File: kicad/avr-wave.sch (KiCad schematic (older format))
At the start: 57 parts, among them J1 MIDI_IN, J2 AVR-ISP-6, J3 MAIN_CONN, J4 ADC_CONN, J5 LINE_OUT, U1 L78L05_SO8, U2 6N137, U3 ATmega328-AU, U4 MCP4921, U5 MCP6001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

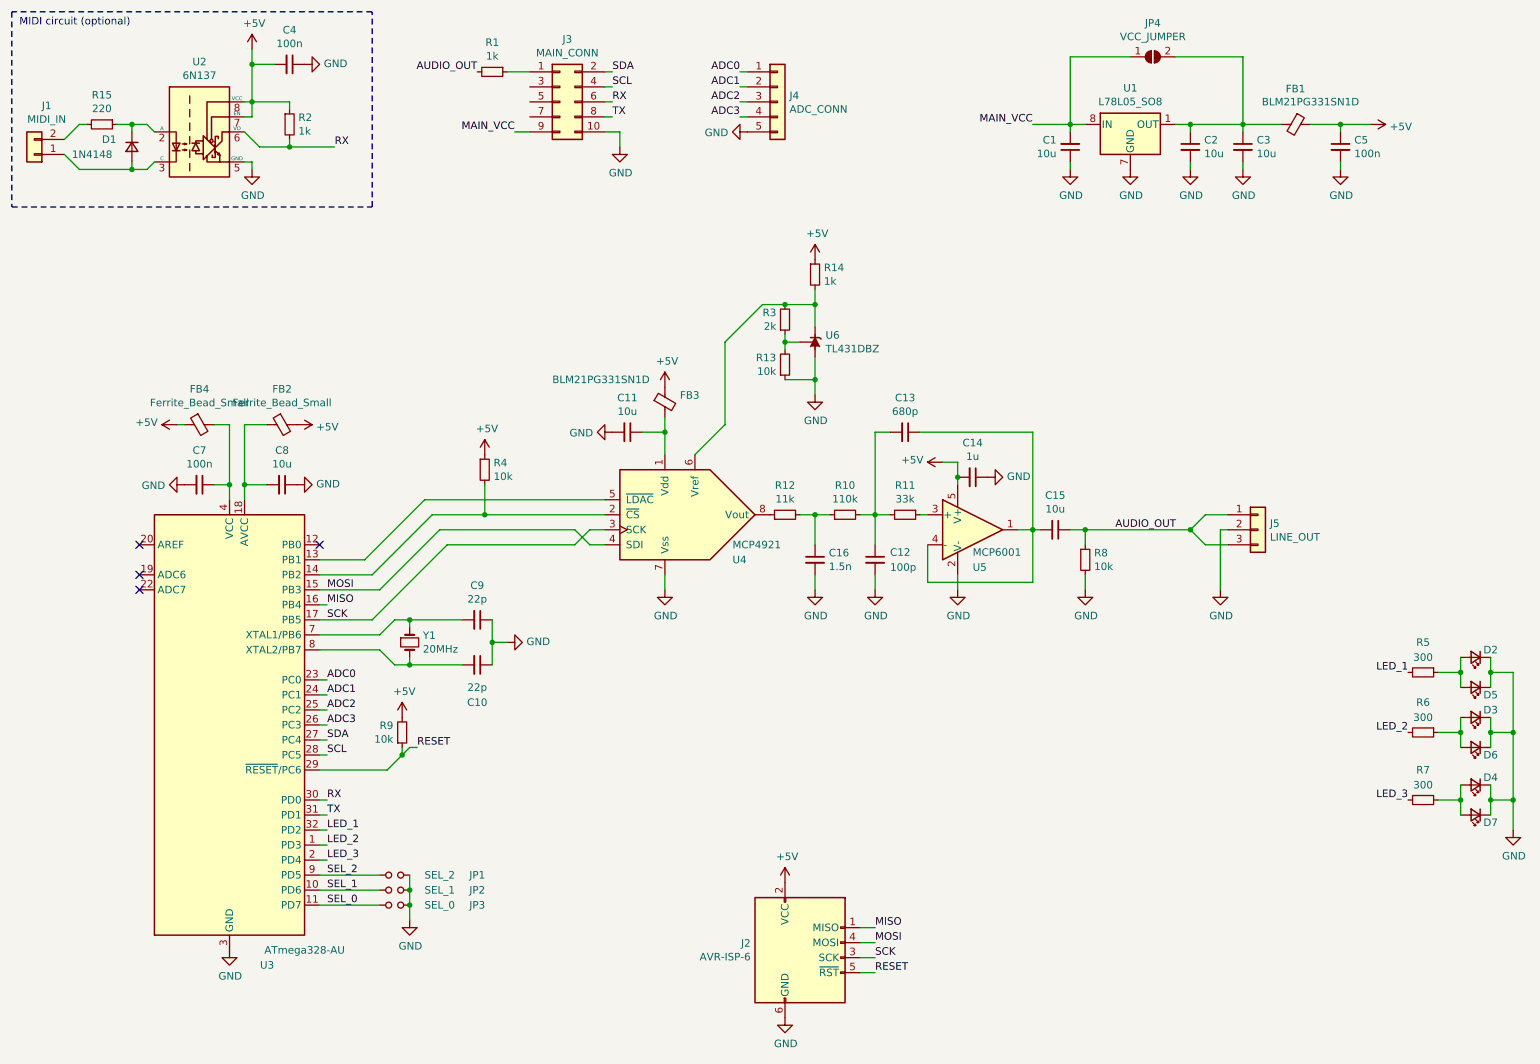
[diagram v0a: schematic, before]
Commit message: Improve power supply filtering
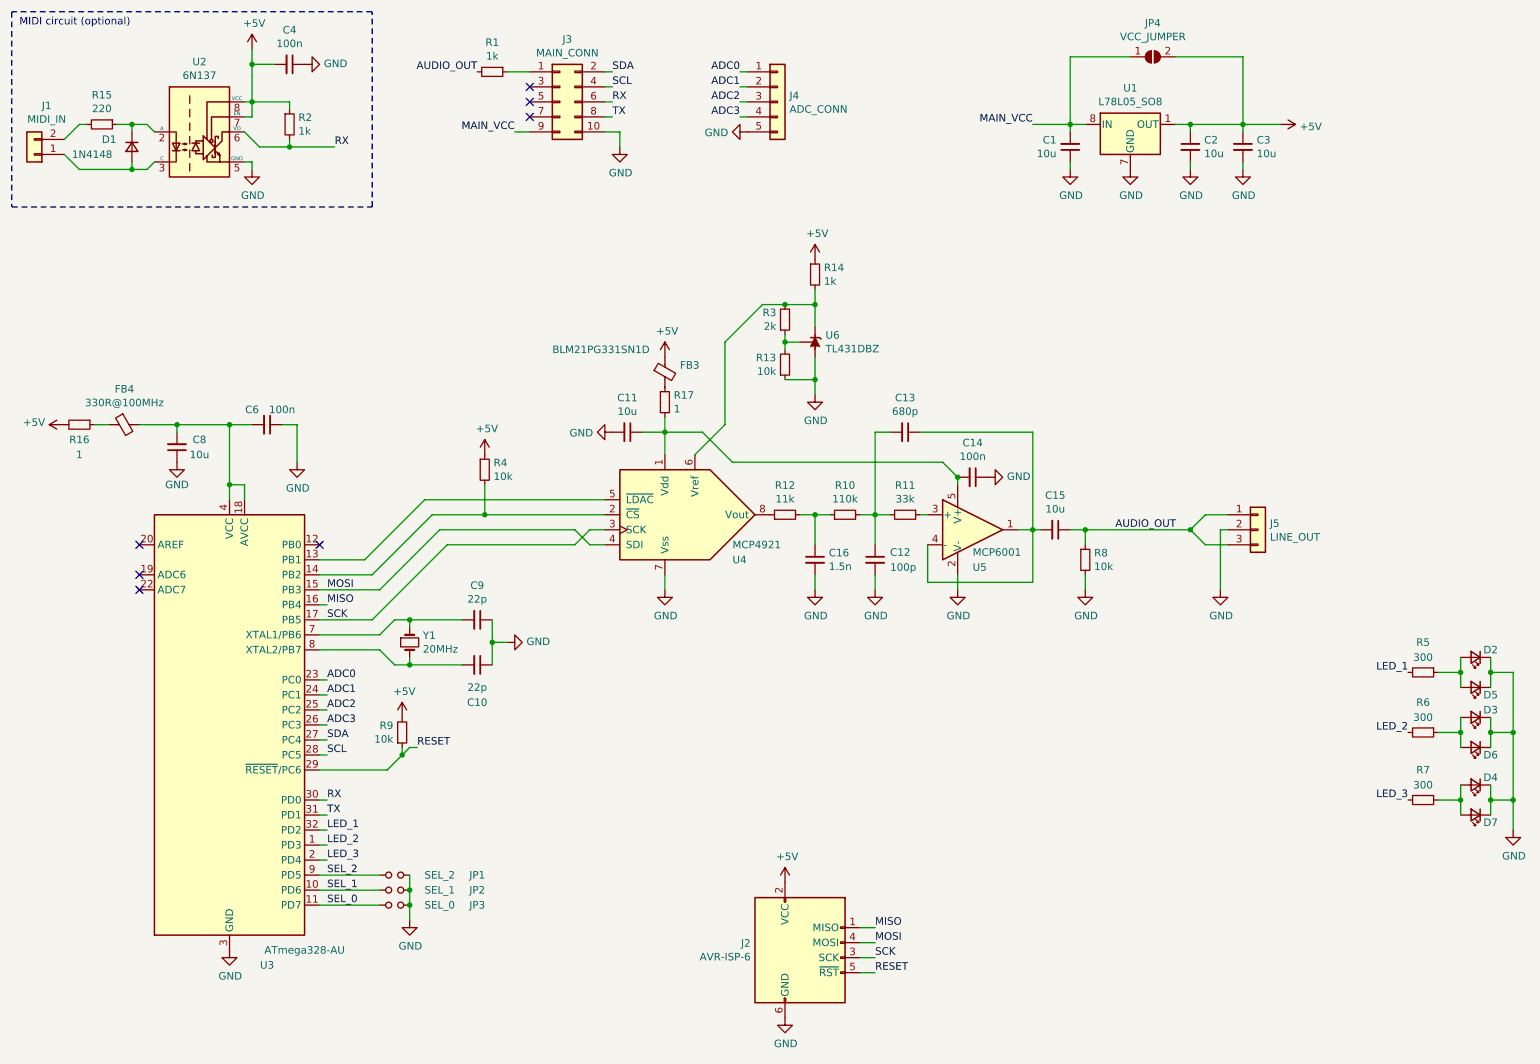
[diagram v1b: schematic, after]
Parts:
- removed C5, C7: 100n, Capacitor_SMD:C_0805_2012Metric, symbol Device:C_Small
- removed FB1: BLM21PG331SN1D, Inductor_SMD:L_0805_2012Metric, symbol Device:Ferrite_Bead_Small
- removed FB2: Ferrite_Bead_Small, Inductor_SMD:L_0805_2012Metric, symbol Device:Ferrite_Bead_Small
- added C6: 100n, Capacitor_SMD:C_0805_2012Metric, symbol Device:C_Small
- added R16, R17: 1, Resistor_SMD:R_0805_2012Metric, symbol Device:R_Small
- C14: value 1u -> 100n
- FB4: value Ferrite_Bead_Small -> 330R@100MHz
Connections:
- net +5V: now also C2.1, C3.1, JP4.2 (B), U1.1 (OUT), R16.2; no longer C14.2, FB4.1, U5.5 (V+)
- net GND: now also C6.1
- net at C8.2, U3.18 (AVCC): now also FB4.2, U3.4 (VCC), U3.6 (VCC), C6.2
- net at C11.1, U4.1 (Vdd): now also C14.2, U5.5 (V+), R17.2; no longer FB3.2
- new net: FB3.2, R17.1
- new net: FB4.1, R16.1
- no-connect marks 4 -> 7
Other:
- moved on the sheet: C8, FB3, FB4
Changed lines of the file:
@@
 Title "DS-50 Digital Synthesizer"
 Date "2020-03-19"
-Rev "1"
+Rev "2"
 Comp "Jacek Wieczorek"
 Comment1 ""
@@
 L Device:Ferrite_Bead_Small FB3
 U 1 1 5E2181EF
-P 5100 3300
-F 0 "FB3" H 5200 3346 50  0000 L CNN
-F 1 "BLM21PG331SN1D" H 4350 3450 50  0000 L CNN
-F 2 "Inductor_SMD:L_0805_2012Metric" V 5030 3300 50  0001 C CNN
-F 3 "~" H 5100 3300 50  0001 C CNN
-	1    5100 3300
+P 5100 3100
+F 0 "FB3" H 5200 3146 50  0000 L CNN
+F 1 "BLM21PG331SN1D" H 4350 3250 50  0000 L CNN
+F 2 "Inductor_SMD:L_0805_2012Metric" V 5030 3100 50  0001 C CNN
+F 3 "~" H 5100 3100 50  0001 C CNN
+	1    5100 3100
 	1    0    0    -1
 $EndComp
@@
 L power:+5V #PWR0102
 U 1 1 5E21AA1F
-P 5100 3200
-F 0 "#PWR0102" H 5100 3050 50  0001 C CNN
-F 1 "+5V" H 5115 3373 50  0000 C CNN
-F 2 "" H 5100 3200 50  0001 C CNN
-F 3 "" H 5100 3200 50  0001 C CNN
-	1    5100 3200
+P 5100 3000
+F 0 "#PWR0102" H 5100 2850 50  0001 C CNN
+F 1 "+5V" H 5115 3173 50  0000 C CNN
+F 2 "" H 5100 3000 50  0001 C CNN
+F 3 "" H 5100 3000 50  0001 C CNN
+	1    5100 3000
 	1    0    0    -1
 $EndComp
@@
 	1    5100 4550
 	1    0    0    -1
-$EndComp
-$Comp
-L Device:Ferrite_Bead_Small FB2
-U 1 1 5E21F619
-P 2550 3450
-F 0 "FB2" V 2313 3450 50  0000 C CNN
-F 1 "Ferrite_Bead_Small" V 2404 3450 50  0000 C CNN
-F 2 "Inductor_SMD:L_0805_2012Metric" V 2480 3450 50  0001 C CNN
-F 3 "~" H 2550 3450 50  0001 C CNN
-	1    2550 3450
-	0    -1   1    0
-$EndComp
-$Comp
-L Device:C_Small C7
-U 1 1 5E220B18
-P 2000 3850
-F 0 "C7" V 2229 3850 50  0000 C CNN
-F 1 "100n" V 2138 3850 50  0000 C CNN
-F 2 "Capacitor_SMD:C_0805_2012Metric" H 2000 3850 50  0001 C CNN
-F 3 "~" H 2000 3850 50  0001 C CNN
-	1    2000 3850
-	0    1    -1   0
 $EndComp
 Wire Wire Line
@@
 Wire Wire Line
 	7800 1450 7800 1500
-$Comp
-L Device:Ferrite_Bead_Small FB1
-U 1 1 5E229C00
-P 9300 1450
-F 0 "FB1" V 9063 1450 50  0000 C CNN
-F 1 "BLM21PG331SN1D" V 9150 1550 50  0000 C CNN
-F 2 "Inductor_SMD:L_0805_2012Metric" V 9230 1450 50  0001 C CNN
-F 3 "~" H 9300 1450 50  0001 C CNN
-	1    9300 1450
-	0    1    1    0
-$EndComp
 Wire Wire Line
 	9200 1450 8950 1450
 Connection ~ 8950 1450
 $Comp
-L Device:C_Small C5
-U 1 1 5E22AEE1
-P 9600 1600
-F 0 "C5" H 9692 1646 50  0000 L CNN
-F 1 "100n" H 9692 1555 50  0000 L CNN
-F 2 "Capacitor_SMD:C_0805_2012Metric" H 9600 1600 50  0001 C CNN
-F 3 "~" H 9600 1600 50  0001 C CNN
-	1    9600 1600
-	1    0    0    -1
-$EndComp
-Wire Wire Line
-	9600 1500 9600 1450
-Wire Wire Line
-	9600 1450 9400 1450
-$Comp
-L power:GND #PWR0109
-U 1 1 5E22C38C
-P 9600 1750
-F 0 "#PWR0109" H 9600 1500 50  0001 C CNN
-F 1 "GND" H 9605 1577 50  0000 C CNN
-F 2 "" H 9600 1750 50  0001 C CNN
-F 3 "" H 9600 1750 50  0001 C CNN
-	1    9600 1750
-	1    0    0    -1
-$EndComp
-Wire Wire Line
-	9600 1750 9600 1700
-$Comp
 L power:+5V #PWR0110
 U 1 1 5E22D971
-P 9800 1450
-F 0 "#PWR0110" H 9800 1300 50  0001 C CNN
-F 1 "+5V" V 9815 1578 50  0000 L CNN
-F 2 "" H 9800 1450 50  0001 C CNN
-F 3 "" H 9800 1450 50  0001 C CNN
-	1    9800 1450
-	0    1    1    0
-$EndComp
-Wire Wire Line
-	9600 1450 9800 1450
-Connection ~ 9600 1450
+P 9200 1450
+F 0 "#PWR0110" H 9200 1300 50  0001 C CNN
+F 1 "+5V" V 9215 1578 50  0000 L CNN
+F 2 "" H 9200 1450 50  0001 C CNN
+F 3 "" H 9200 1450 50  0001 C CNN
+	1    9200 1450
+	0    1    1    0
+$EndComp
 $Comp
 L Device:C_Small C8
 U 1 1 5E23482B
-P 2550 3850
-F 0 "C8" V 2779 3850 50  0000 C CNN
-F 1 "10u" V 2688 3850 50  0000 C CNN
-F 2 "Capacitor_SMD:C_0805_2012Metric" H 2550 3850 50  0001 C CNN
-F 3 "~" H 2550 3850 50  0001 C CNN
-	1    2550 3850
-	0    1    -1   0
-$EndComp
-Wire Wire Line
-	2300 3950 2300 3850
-Wire Wire Line
-	2450 3850 2300 3850
-Wire Wire Line
-	2100 3850 2200 3850
-Wire Wire Line
-	2200 3850 2200 3950
-$Comp
-L power:GND #PWR0111
-U 1 1 5E23A430
-P 1900 3850
-F 0 "#PWR0111" H 1900 3600 50  0001 C CNN
-F 1 "GND" V 1905 3722 50  0000 R CNN
-F 2 "" H 1900 3850 50  0001 C CNN
-F 3 "" H 1900 3850 50  0001 C CNN
-	1    1900 3850
-	0    1    1    0
-$EndComp
-$Comp
-L power:GND #PWR0112
-U 1 1 5E23A715
-P 2650 3850
-F 0 "#PWR0112" H 2650 3600 50  0001 C CNN
-F 1 "GND" V 2655 3722 50  0000 R CNN
-F 2 "" H 2650 3850 50  0001 C CNN
-F 3 "" H 2650 3850 50  0001 C CNN
-	1    2650 3850
-	0    -1   -1   0
-$EndComp
-Wire Wire Line
-	2450 3450 2300 3450
-Wire Wire Line
-	2300 3450 2300 3850
-Connection ~ 2300 3850
-$Comp
-L power:+5V #PWR0113
-U 1 1 5E2405B9
-P 2650 3450
-F 0 "#PWR0113" H 2650 3300 50  0001 C CNN
-F 1 "+5V" V 2665 3578 50  0000 L CNN
-F 2 "" H 2650 3450 50  0001 C CNN
-F 3 "" H 2650 3450 50  0001 C CNN
-	1    2650 3450
-	0    1    1    0
+P 1850 3600
+F 0 "C8" H 2000 3550 50  0000 C CNN
+F 1 "10u" H 2000 3650 50  0000 C CNN
+F 2 "Capacitor_SMD:C_0805_2012Metric" H 1850 3600 50  0001 C CNN
+F 3 "~" H 1850 3600 50  0001 C CNN
+	1    1850 3600
+	1    0    0    1
 $EndComp
 $Comp
 L power:+5V #PWR0114
 U 1 1 5E240A04
-P 1850 3450
-F 0 "#PWR0114" H 1850 3300 50  0001 C CNN
-F 1 "+5V" V 1865 3578 50  0000 L CNN
-F 2 "" H 1850 3450 50  0001 C CNN
-F 3 "" H 1850 3450 50  0001 C CNN
-	1    1850 3450
+P 1100 3450
+F 0 "#PWR0114" H 1100 3300 50  0001 C CNN
+F 1 "+5V" V 1115 3578 50  0000 L CNN
+F 2 "" H 1100 3450 50  0001 C CNN
+F 3 "" H 1100 3450 50  0001 C CNN
+	1    1100 3450
 	0    -1   -1   0
 $EndComp
-Wire Wire Line
-	2200 3450 2200 3850
-Connection ~ 2200 3850
 $Comp
 L Connector:AVR-ISP-6 J2
@@
 Connection ~ 7050 3800
 Wire Wire Line
-	7050 3700 7050 3800
-Wire Wire Line
-	6950 3700 7050 3700
-Wire Wire Line
 	7050 3850 7050 3800
 $Comp
@@
 P 7150 3800
 F 0 "C14" V 6921 3800 50  0000 C CNN
-F 1 "1u" V 7012 3800 50  0000 C CNN
+F 1 "100n" V 7012 3800 50  0000 C CNN
 F 2 "Capacitor_SMD:C_0805_2012Metric" H 7150 3800 50  0001 C CNN
 F 3 "~" H 7150 3800 50  0001 C CNN
 	1    7150 3800
 	0    1    1    0
-$EndComp
-$Comp
-L power:+5V #PWR0130
-U 1 1 5E3FAA66
-P 6950 3700
-F 0 "#PWR0130" H 6950 3550 50  0001 C CNN
-F 1 "+5V" V 6965 3828 50  0000 L CNN
-F 2 "" H 6950 3700 50  0001 C CNN
-F 3 "" H 6950 3700 50  0001 C CNN
-	1    6950 3700
-	0    -1   -1   0
 $EndComp
 Wire Wire Line
@@
 L Device:Ferrite_Bead_Small FB4
 U 1 1 5E85A540
-P 2000 3450
-F 0 "FB4" V 1763 3450 50  0000 C CNN
-F 1 "Ferrite_Bead_Small" V 1854 3450 50  0000 C CNN
-F 2 "Inductor_SMD:L_0805_2012Metric" V 1930 3450 50  0001 C CNN
-F 3 "~" H 2000 3450 50  0001 C CNN
-	1    2000 3450
+P 1500 3450
+F 0 "FB4" V 1263 3450 50  0000 C CNN
+F 1 "330R@100MHz" V 1354 3450 50  0000 C CNN
+F 2 "Inductor_SMD:L_0805_2012Metric" V 1430 3450 50  0001 C CNN
+F 3 "~" H 1500 3450 50  0001 C CNN
+	1    1500 3450
 	0    -1   1    0
 $EndComp
-Wire Wire Line
-	2100 3450 2200 3450
-Wire Wire Line
-	1900 3450 1850 3450
 $Comp
 L Device:LED_Small D5
@@
 	1450 1450 1550 1450
 Connection ~ 1550 1450
+$Comp
+L Device:R_Small R17
+U 1 1 5EDF3724
+P 5100 3300
+F 0 "R17" H 5159 3346 50  0000 L CNN
+F 1 "1" H 5159 3255 50  0000 L CNN
+F 2 "Resistor_SMD:R_0805_2012Metric" H 5100 3300 50  0001 C CNN
+F 3 "~" H 5100 3300 50  0001 C CNN
+	1    5100 3300
+	1    0    0    -1
+$EndComp
+$Comp
+L Device:R_Small R16
+U 1 1 5EE282B6
+P 1200 3450
+F 0 "R16" V 1300 3450 50  0000 C CNN
+F 1 "1" V 1400 3450 50  0000 C CNN
+F 2 "Resistor_SMD:R_0805_2012Metric" H 1200 3450 50  0001 C CNN
+F 3 "~" H 1200 3450 50  0001 C CNN
+	1    1200 3450
+	0    1    1    0
+$EndComp
+Wire Wire Line
+	1300 3450 1400 3450
+Wire Wire Line
+	1850 3500 1850 3450
+Wire Wire Line
+	1600 3450 1850 3450
+$Comp
+L power:GND #PWR0111
+U 1 1 5EE9AC7C
+P 1850 3700
+F 0 "#PWR0111" H 1850 3450 50  0001 C CNN
+F 1 "GND" H 1850 3550 50  0000 C CNN
+F 2 "" H 1850 3700 50  0001 C CNN
+F 3 "" H 1850 3700 50  0001 C CNN
+	1    1850 3700
+	1    0    0    -1
+$EndComp
+$Comp
+L Device:C_Small C6
+U 1 1 5EEADFE3
+P 2450 3450
+F 0 "C6" V 2550 3350 50  0000 C CNN
+F 1 "100n" V 2550 3550 50  0000 C CNN
+F 2 "Capacitor_SMD:C_0805_2012Metric" H 2450 3450 50  0001 C CNN
+F 3 "~" H 2450 3450 50  0001 C CNN
+	1    2450 3450
+	0    1    -1   0
+$EndComp
+Wire Wire Line
+	2350 3450 2200 3450
+$Comp
+L power:GND #PWR0112
+U 1 1 5EEC8E69
+P 2650 3700
+F 0 "#PWR0112" H 2650 3450 50  0001 C CNN
+F 1 "GND" H 2655 3527 50  0000 C CNN
+F 2 "" H 2650 3700 50  0001 C CNN
+F 3 "" H 2650 3700 50  0001 C CNN
+	1    2650 3700
+	1    0    0    -1
+$EndComp
+Wire Wire Line
+	2650 3700 2650 3450
+Wire Wire Line
+	2650 3450 2550 3450
+Wire Wire Line
+	1850 3450 2200 3450
+Connection ~ 1850 3450
+Wire Wire Line
+	2300 3950 2300 3850
+Wire Wire Line
+	2300 3850 2200 3850
+Connection ~ 2200 3850
+Wire Wire Line
+	2200 3850 2200 3950
+NoConn ~ 4200 1200
+NoConn ~ 4200 1300
+NoConn ~ 4200 1400
+Wire Wire Line
+	5100 3500 5350 3500
+Wire Wire Line
+	5350 3500 5550 3700
+Wire Wire Line
+	5550 3700 6950 3700
+Wire Wire Line
+	7050 3800 6950 3700
+Wire Wire Line
+	2200 3450 2200 3850
+Connection ~ 2200 3450
 $EndSCHEMATC

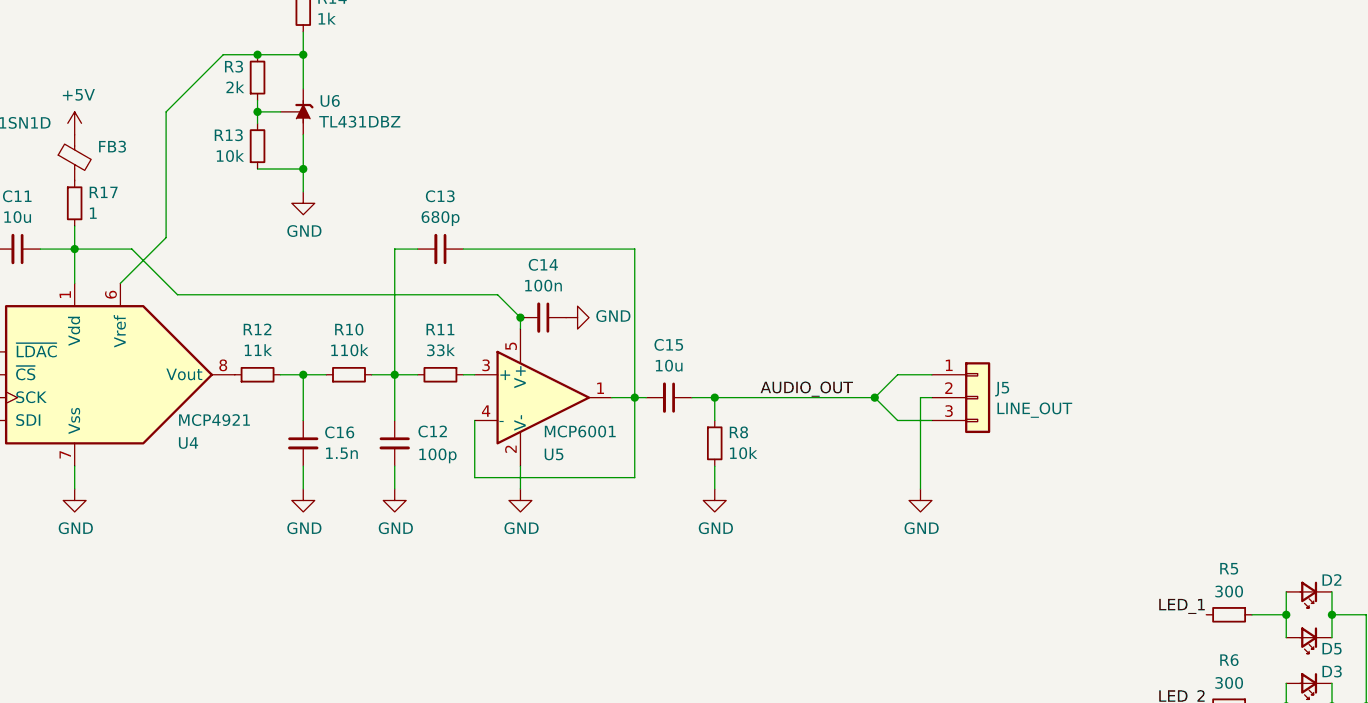
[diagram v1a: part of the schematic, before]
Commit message: Fix Sallen-Key filter, minor PCB improvements
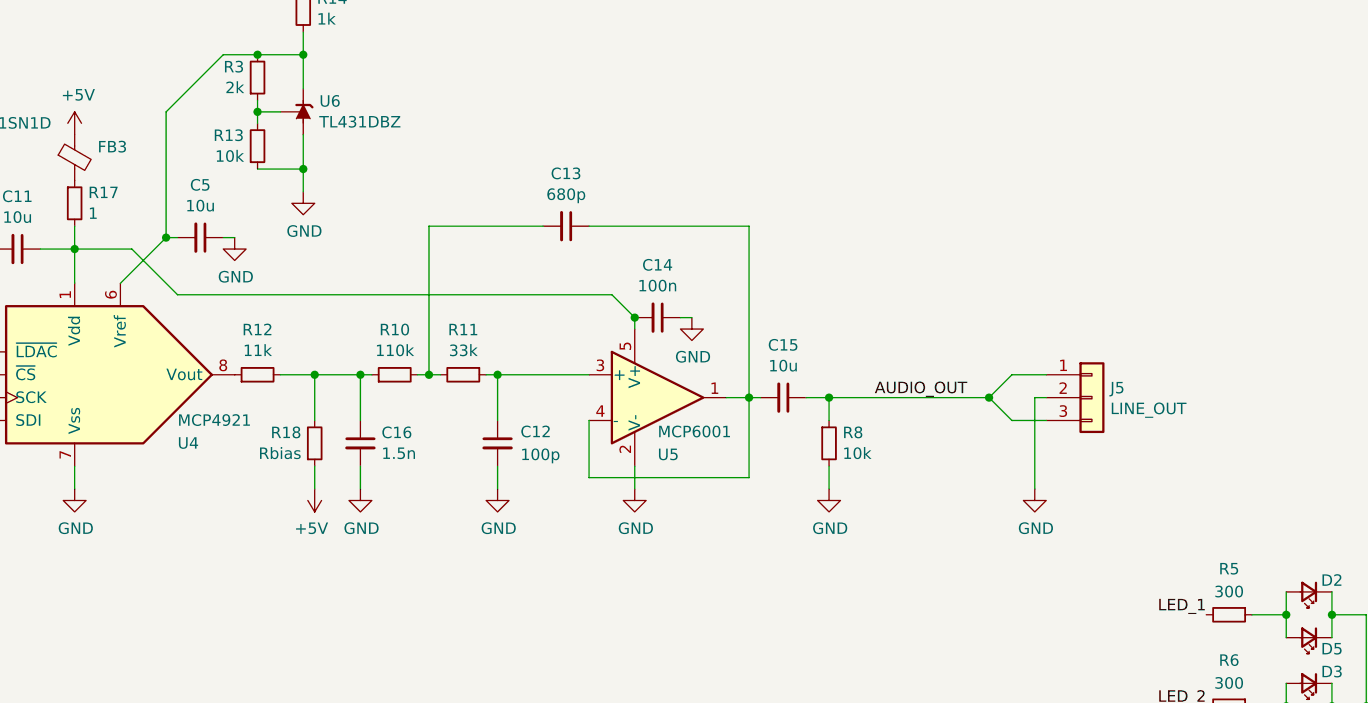
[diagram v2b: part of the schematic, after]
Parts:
- added C5: 10u, Capacitor_SMD:C_0805_2012Metric, symbol Device:C_Small
- added R18: Rbias, Resistor_SMD:R_0805_2012Metric, symbol Device:R_Small
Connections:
- net +5V: now also R18.1
- net GND: now also C5.1
- net at R14.2, R3.2, U4.6 (Vref)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: now also C5.2
- net at R11.1, U5.3 (+): now also C12.1
- net at C13.2, R10.2, R11.2: no longer C12.1
- net at C16.1, R10.1, R12.2: now also R18.2
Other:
- moved on the sheet: C12, C13, C14, C15, C16, J5, R10, R11, R8, U5
